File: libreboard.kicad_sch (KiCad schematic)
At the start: 78 parts, among them J100 Screw Terminal, J101 Screw Terminal, J11 USB_C_Receptacle_USB2.0, J51 12V Fan 1, J52 12V Fan 2, J53 12V Fan 3, J54 12V Fan 4, U10 EMC2305-x-AP, U14 TPS552892QWRYQRQ1, U4 TPS552892QWRYQRQ1

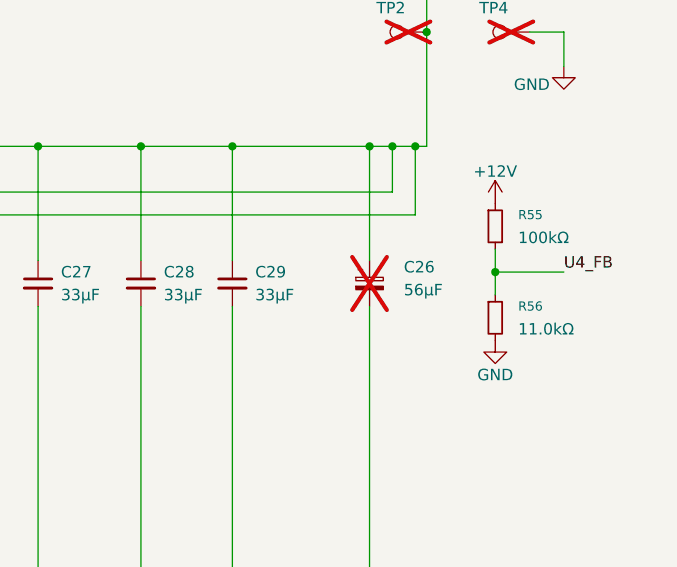
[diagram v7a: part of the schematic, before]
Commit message: C26: fit again, as APAQ 250AVCP470M0506 47 uF 25 V polymer
C26 (bulk polymer on +12V, U4's output) was fitted on Rev1 but became
DNP in 82c34c4, the KiCad 10 re-save, where it was the only DNP flag
that changed - an accident, so JLC's placement left it empty. Fitted
again. The Panasonic 20SVPF56MX (C2162042) has 2 at JLC with a minimum
order of 6; the APAQ part (C54864098, 1,035 at JLC) is the only 5 mm
polymer can in stock: 47 uF, 25 V, 35 mOhm, same footprint.
ERC, DRC and schematic parity unchanged.

Co-Authored-By: Claude Opus 5.5 <noreply@anthropic.com>
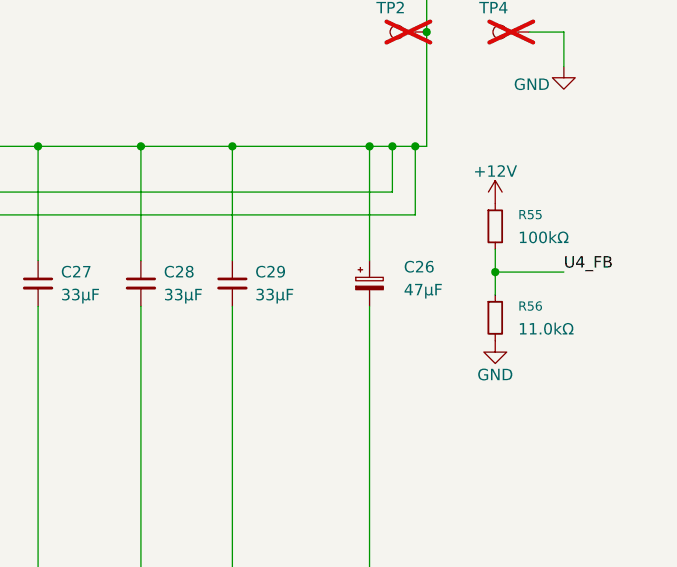
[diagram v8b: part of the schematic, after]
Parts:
- C26: value 56µF -> 47µF; Dist. P/N P122099TR-ND -> C54864098; Distributor Digikey -> LCSC; LCSC C2162042 -> C54864098; Manf. P/N 20SVF56M -> 250AVCP470M0506; Manufacturer Panasonic -> APAQ Technology; Part Description Capacitor, Aluminum, 56µF, ±20%, 20V, 30mΩ ESR -> Capacitor, Polymer Aluminum, 47µF, ±20%, 25V, 35mΩ ESR, D5x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; now fitted
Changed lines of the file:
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@@
 		(on_board yes)
 		(in_pos_files yes)
-		(dnp yes)
+		(dnp no)
 		(fields_autoplaced yes)
 		(property "Reference" "C26"
@@
 			)
 		)
-		(property "Value" "56µF"
+		(property "Value" "47µF"
 			(at 307.34 233.1338 0)
 			(show_name no)
@@
 			)
 		)
-		(property "Dist. P/N" "P122099TR-ND"
+		(property "Dist. P/N" "C54864098"
 			(at 303.53 232.41 0)
 			(hide yes)
@@
 			)
 		)
-		(property "Distributor" "Digikey"
+		(property "Distributor" "LCSC"
 			(at 303.53 232.41 0)
 			(hide yes)
@@
 			)
 		)
-		(property "Manf. P/N" "20SVF56M"
+		(property "Manf. P/N" "250AVCP470M0506"
 			(at 303.53 232.41 0)
 			(hide yes)
@@
 			)
 		)
-		(property "Manufacturer" "Panasonic"
+		(property "Manufacturer" "APAQ Technology"
 			(at 303.53 232.41 0)
 			(hide yes)
@@
 			)
 		)
-		(property "Part Description" "Capacitor, Aluminum, 56µF, ±20%, 20V, 30mΩ ESR"
+		(property "Part Description" "Capacitor, Polymer Aluminum, 47µF, ±20%, 25V, 35mΩ ESR, D5x5.8mm"
 			(at 303.53 232.41 0)
 			(hide yes)
@@
 			)
 		)
-		(property "LCSC" "C2162042"
+		(property "LCSC" "C54864098"
 			(at 303.53 232.41 0)
 			(hide yes)
